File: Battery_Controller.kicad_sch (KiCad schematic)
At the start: 1 part, among them U1 BQ25895RTWR

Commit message: Prepared for Meeting
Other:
- removed sheet c
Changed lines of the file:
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@@
-		)
-	)
-	(sheet
-		(at 85.725 64.135)
-		(size 38.735 30.48)
-		(exclude_from_sim no)
-		(in_bom yes)
-		(on_board yes)
-		(dnp no)
-		(fields_autoplaced yes)
-		(stroke
-			(width 0.1524)
-			(type solid)
-		)
-		(fill
-			(color 0 0 0 0)
-		)
-		(property "Sheetname" "c"
-			(at 85.725 63.4234 0)
-			(show_name yes)
-			(do_not_autoplace no)
-			(effects
-				(font
-					(size 1.27 1.27)
-				)
-				(justify left bottom)
-			)
-		)
-		(property "Sheetfile" "Capacitor.kicad_sch"
-			(at 85.725 95.1996 0)
-			(show_name no)
-			(do_not_autoplace no)
-			(effects
-				(font
-					(size 1.27 1.27)
-				)
-				(justify left top)
-			)
-		)
-		(instances
-			(project "Solar_Battery"
-				(path "/6805959e-39bb-4644-b93e-3970e29fedc0/49420c5f-19b8-4027-9796-8766afa78876"
-					(page "7")
-				)
-			)
 		)
 	)

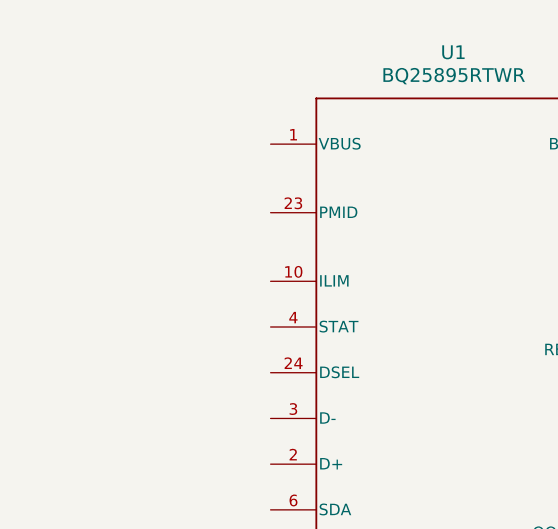
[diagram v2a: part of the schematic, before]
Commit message: Added some symbols to top part
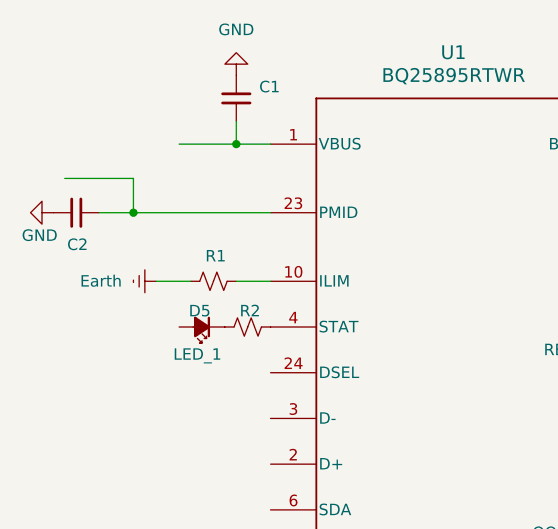
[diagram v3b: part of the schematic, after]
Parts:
- added C1: C_Small, symbol Device:C_Small
- added C2: C_Small, Package_SO:SOIC-8_3.9x4.9mm_P1.27mm, symbol Device:C_Small
- added D5: LED_1, OptoDevice:R_LDR_D6.4mm_P3.4mm_Vertical, symbol Device:LED_Small_Filled
- added R1, R2: R_Small_US, symbol Device:R_Small_US
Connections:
- net at U1.1 (VBUS): now also C1.2
- net at U1.10 (ILIM): now also R1.2
- net at U1.23 (PMID): now also C2.1
- net at U1.4 (STAT): now also R2.2
- new net: D5.1 (K), R2.1
- new net Earth: R1.1
- new net GND: C1.1, C2.2

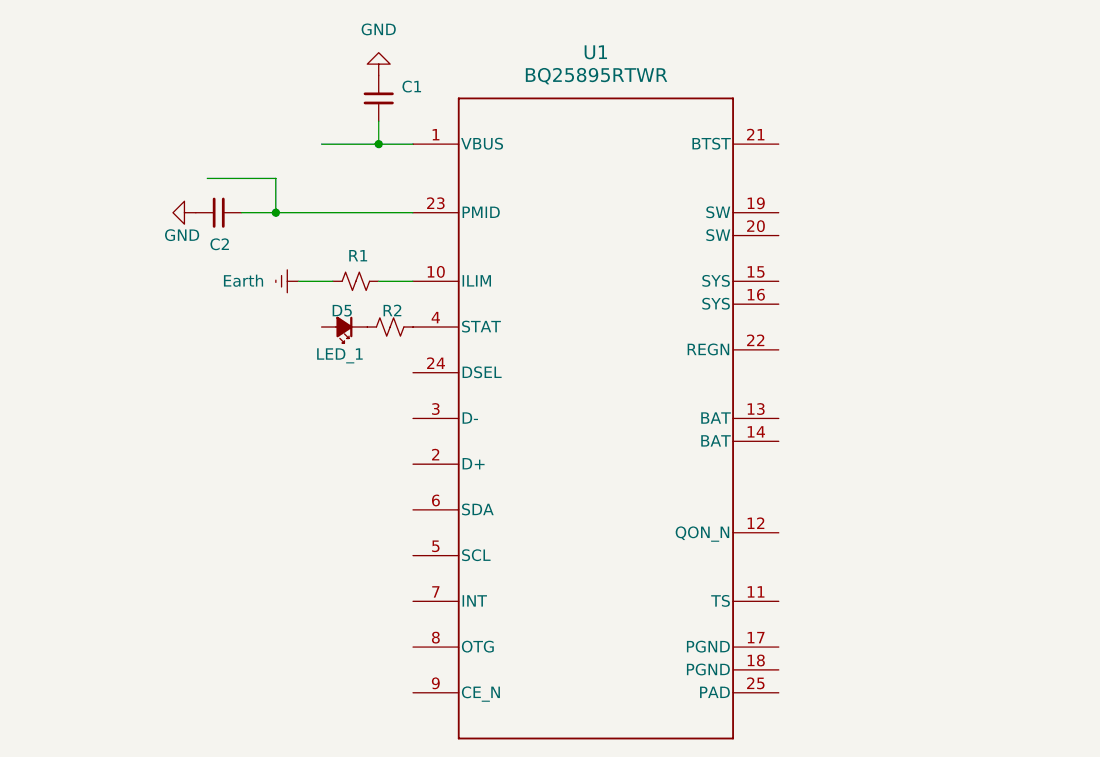
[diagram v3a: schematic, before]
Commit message: Most of the symbols in BQ
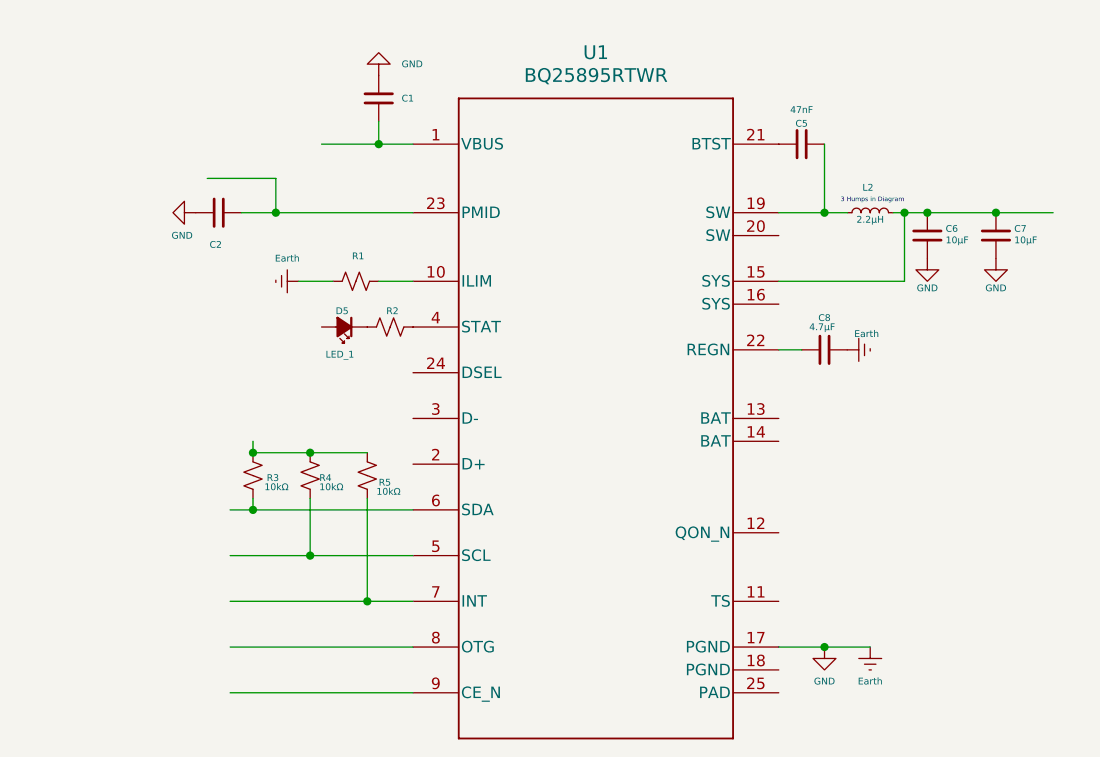
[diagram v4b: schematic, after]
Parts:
- added C5: 47nF, Package_SO:SOIC-8_3.9x4.9mm_P1.27mm, symbol Device:C_Small
- added C6, C7: 10µF, Package_SO:SOIC-8_3.9x4.9mm_P1.27mm, symbol Device:C_Small
- added C8: 4.7µF, symbol Device:C_Small
- added L2: 2.2µH, Inductor_SMD:L_CommonModeChoke_Coilcraft_0603USB, symbol Device:L_Small
- added R3, R4, R5: 10kΩ, symbol Device:R_Small_US
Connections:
- net GND is gone; now on net Earth: C1.1, C2.2
- net Earth: now also U1.17 (PGND), C6.2, C7.2, C8.2
- net at U1.15 (SYS): now also C6.1, C7.1, L2.2
- net at U1.19 (SW): now also C5.2, L2.1
- net at U1.21 (BTST): now also C5.1
- net at U1.22 (REGN): now also C8.1
- net at U1.5 (SCL): now also R4.2
- net at U1.6 (SDA): now also R3.2
- net at U1.7 (INT): now also R5.2
- new net: R3.1, R4.1, R5.1
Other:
- note added: "3 Humps in Diagram"

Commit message: Finished BQ Chip
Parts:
- added BT1: Battery_Cell, Package_SO:SOIC-20W_7.5x12.8mm_P1.27mm, symbol Device:Battery_Cell
- added C9: 10uF, symbol Device:C_Small
- added R6: 5.23KΩ, Package_DIP:DIP-8_W7.62mm, symbol Device:R_Small_US
- added R7: 30.1KΩ, Package_DIP:DIP-8_W7.62mm, symbol Device:R_Small_US
- added R8: 10KΩ, symbol Device:R_Small_US
- added SW1: SW_Push, Button_Switch_SMD:SW_SPST_CK_KMS2xxGP, symbol Switch:SW_Push
- C1: value C_Small -> 1µF
- C2: value C_Small -> 40µF
- R1: value R_Small_US -> 260Ω
- R2: value R_Small_US -> 2.2KΩ
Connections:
- net Earth: now also C1.2, U1.1 (VBUS), U1.2 (D+), U1.3 (D-), BT1.2 (-), C9.2, R7.2, R8.2, SW1.2
- net SYS?: now reaches C6.1, C7.1, L2.2, U1.15 (SYS)
- net VREF: now reaches R3.1, R4.1, R5.1
- net Host: now reaches R3.2, U1.6 (SDA)
- net Host: now also R4.2, R5.2, U1.5 (SCL), U1.7 (INT), U1.8 (OTG), U1.9 (CE_N)
- net Phone: now reaches C2.1, U1.23 (PMID)
- net SYS: now reaches D5.2 (A)
- net at U1.11 (TS): now also R6.2, R7.1, R8.1
- net at U1.12 (QON_N): now also SW1.1
- net at U1.14 (BAT): now also BT1.1 (+), C9.1
- net NOT IN DIAGRAM: now reaches U1.24 (DSEL)
- net NOT IN DIAGRAM: now also U1.25 (PAD)
- new net REGN: R6.1
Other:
- note added: "Circles should be completely black"
- note added: "Treating it as /CE"
